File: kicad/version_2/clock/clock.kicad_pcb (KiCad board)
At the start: 2 copper layers, 100 x 100 mm, 34 parts

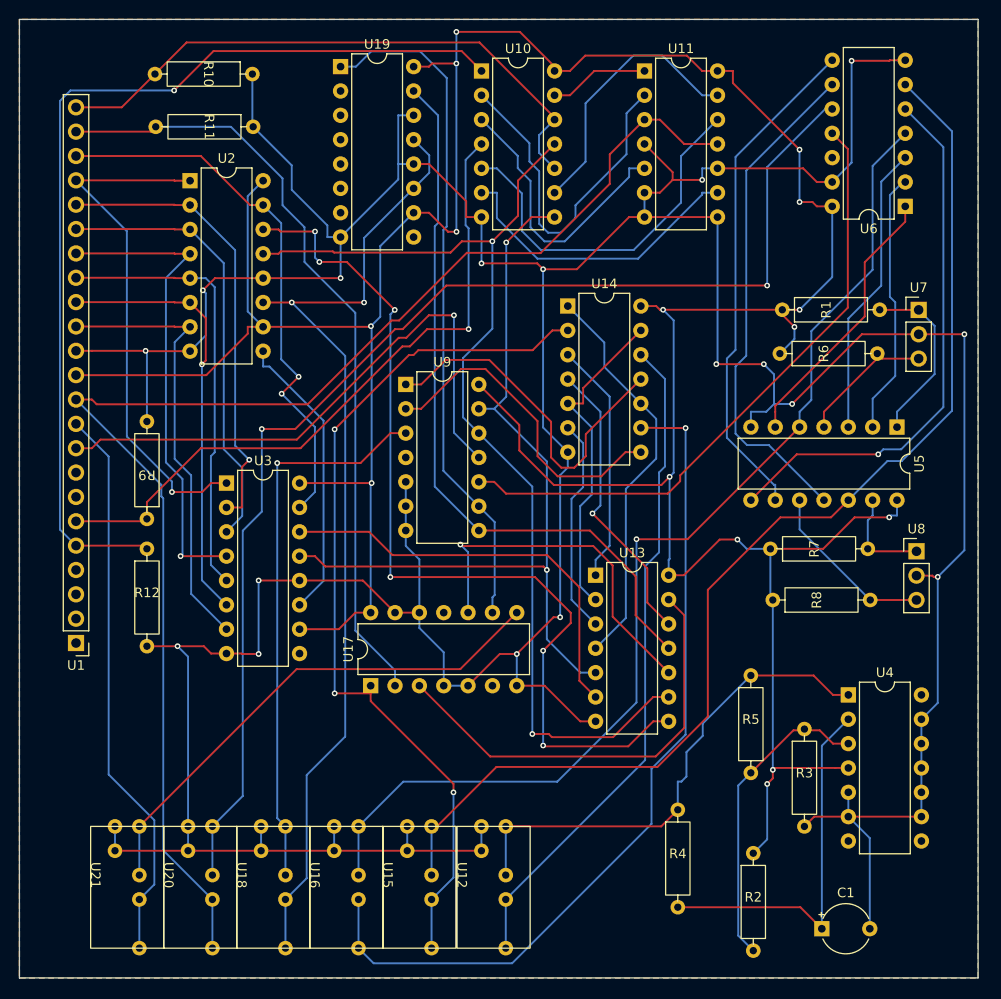
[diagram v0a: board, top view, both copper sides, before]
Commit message: Fixed clock board
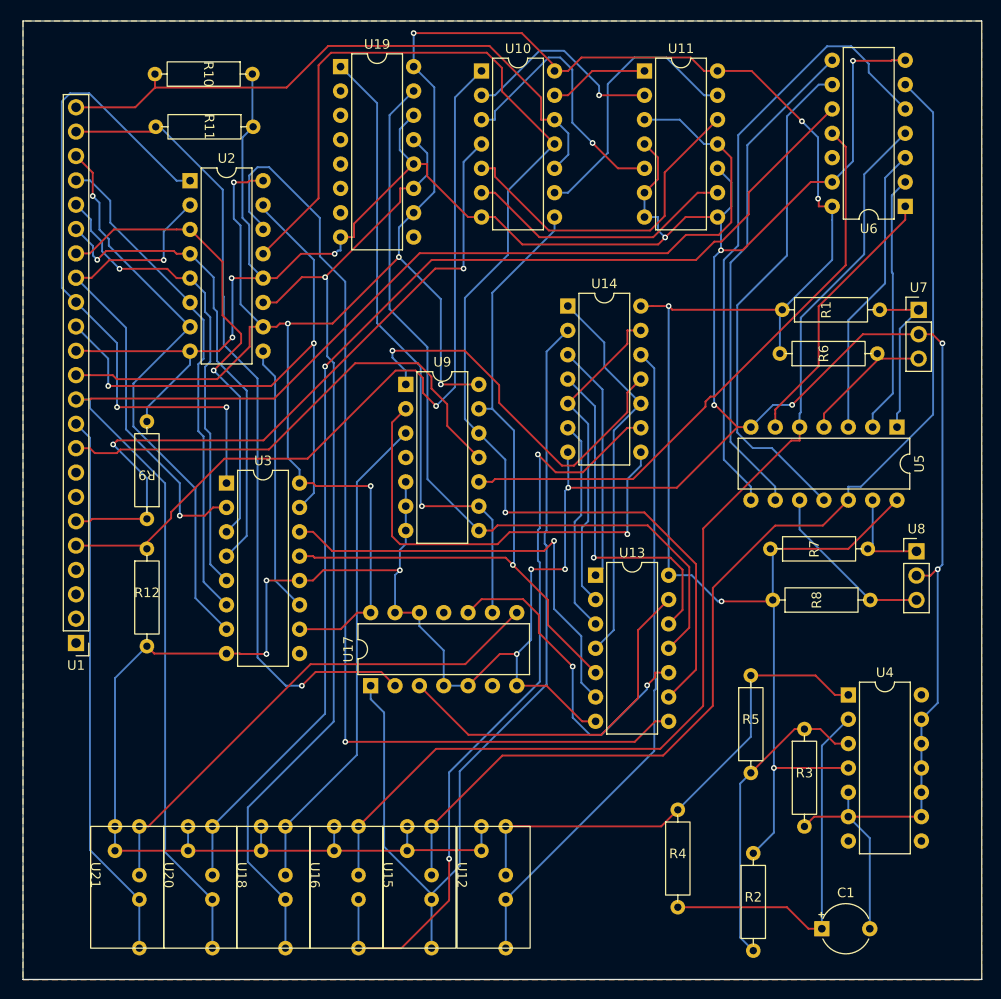
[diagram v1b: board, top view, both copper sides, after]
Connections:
- U2 pad 1: Net-(U1-D6) -> Net-(U1-D1)
- U2 pad 15: Net-(U1-D7) -> Net-(U1-D0)
- U2 pad 2: Net-(U1-D5) -> Net-(U1-D2)
- U2 pad 3: Net-(U1-D4) -> Net-(U1-D3)
- U2 pad 4: Net-(U1-D3) -> Net-(U1-D4)
- U2 pad 5: Net-(U1-D2) -> Net-(U1-D5)
- U2 pad 6: Net-(U1-D1) -> Net-(U1-D6)
- U2 pad 7: Net-(U1-D0) -> Net-(U1-D7)
- U3 pad 1: Net-(U1-D6) -> Net-(U1-D1)
- U3 pad 15: Net-(U1-D7) -> Net-(U1-D0)
- U3 pad 2: Net-(U1-D5) -> Net-(U1-D2)
- U3 pad 3: Net-(U1-D4) -> Net-(U1-D3)
- U3 pad 4: Net-(U1-D3) -> Net-(U1-D4)
- U3 pad 5: Net-(U1-D2) -> Net-(U1-D5)
- U3 pad 6: Net-(U1-D1) -> Net-(U1-D6)
- U3 pad 7: Net-(U1-D0) -> Net-(U1-D7)
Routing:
- net Net-(U1-D1): track 45.4 -> 71.1 mm, vias 1 -> 2
- net Net-(U10-3Q): track 109.1 -> 133.8 mm, vias 2 -> 1
- net Net-(U1-D0): track 46.4 -> 65.3 mm, vias 0 -> 2
- net Net-(U1-WRITE_0): track 101.6 -> 85.3 mm
- net Net-(U10-1B): track 36.5 -> 21.4 mm, vias 0 -> 1
- net Net-(U1-V+): track 351.0 -> 336.2 mm, vias 15 -> 11
- net Net-(U14-4Q): track 34.1 -> 48.5 mm, vias 0 -> 1
- net Net-(U1-CLK_B): track 145.4 -> 157.4 mm
- net Net-(U13-03): track 96.5 -> 106.5 mm, vias 6 -> 1
- net Net-(U14-4B): track 89.8 -> 80.7 mm, vias 1 -> 2
- net Net-(U1-READ_READY): track 61.1 -> 52.2 mm, vias 1 -> 0
- net Net-(U13-I5): track 46.0 -> 38.1 mm
- net Net-(U13-I4): track 76.2 -> 84.1 mm
- net Net-(U5-4Q): track 56.8 -> 64.4 mm, vias 1 -> 0
- net Net-(U18-IN): track 58.0 -> 51.3 mm, vias 1 -> 0
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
